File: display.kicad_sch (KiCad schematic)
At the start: 40 parts, among them J301 ConnectorLCDFrontLight, J302 FPC24(0.5MM), J303 FPC10(0.5MM), Q301 2N7002, Q302 2N7002, Q303 AO3401A

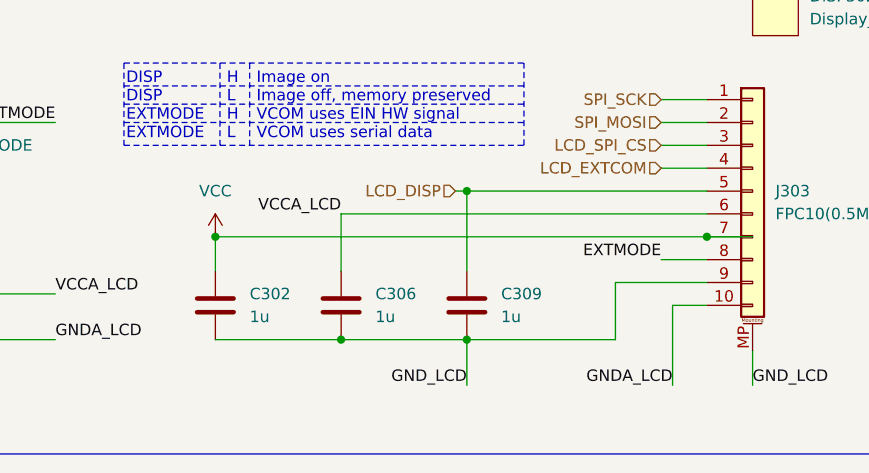
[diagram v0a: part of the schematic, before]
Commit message: schematic: fix LCD VCCA decoupling capacitor
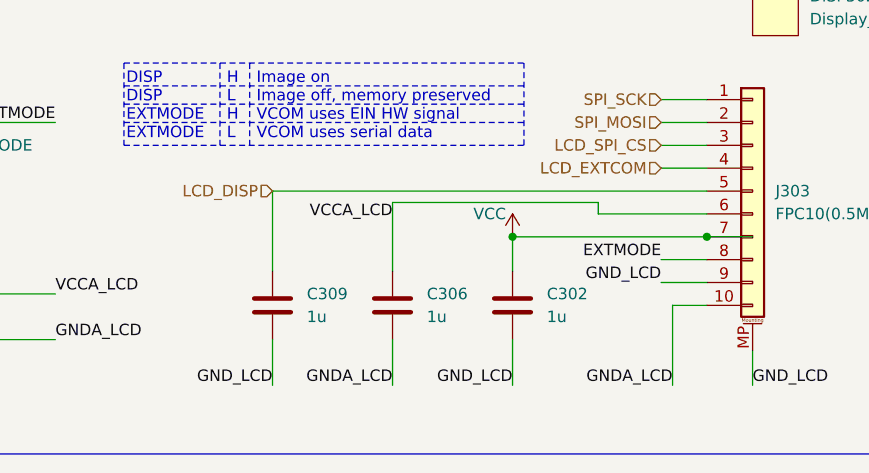
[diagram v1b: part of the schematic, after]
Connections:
- net GNDA_LCD: now also C306.2
- net LCD_CURRENT_SENSE: no longer C306.2
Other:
- moved on the sheet: C302, C306, C309

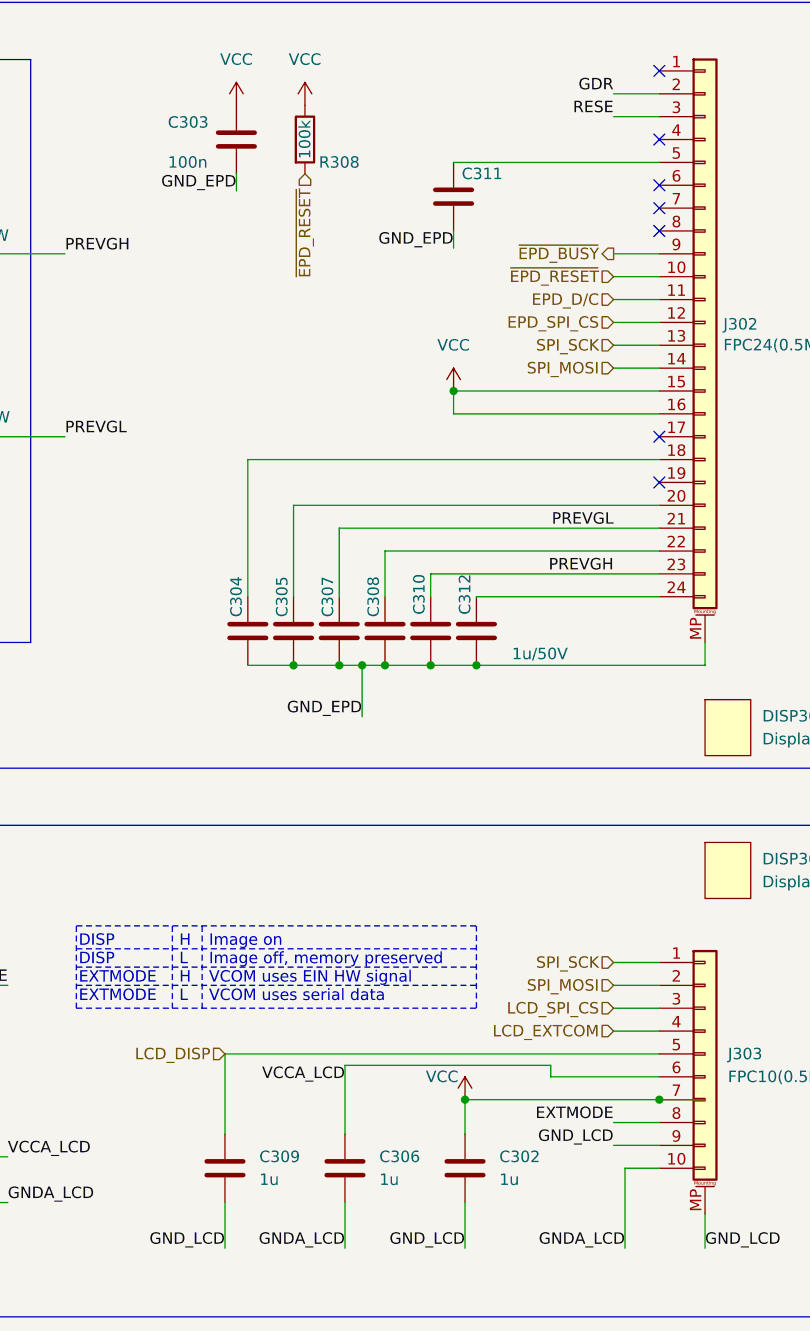
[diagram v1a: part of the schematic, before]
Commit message: Exchange brick-mount holes with actual footprint, connect holes to gnd
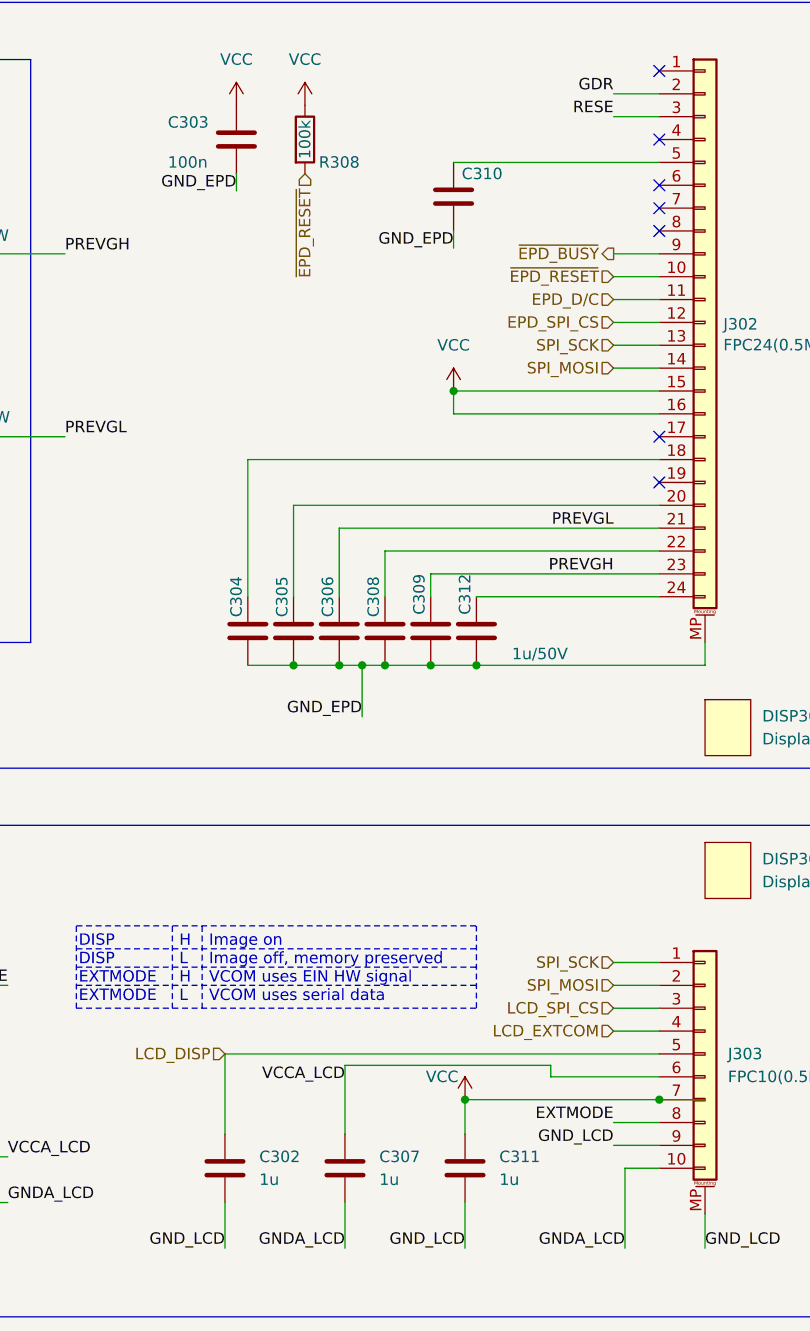
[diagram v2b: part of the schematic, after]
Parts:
- renumbered C309 to C302, C307 to C306, C306 to C307, C310 to C309, C311 to C310, C302 to C311
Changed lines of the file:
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@@
   (symbol (lib_id "Device:C") (at 215.265 148.59 0) (unit 1)
     (in_bom yes) (on_board yes)
-    (property "Reference" "C306" (id 0) (at 219.075 147.3199 0)
+    (property "Reference" "C307" (id 0) (at 219.075 147.3199 0)
       (effects (font (size 1.27 1.27)) (justify left))
     )
@@
   (symbol (lib_id "Device:C") (at 227.33 40.64 0) (unit 1)
     (in_bom yes) (on_board yes)
-    (property "Reference" "C311" (id 0) (at 230.505 38.1 0))
+    (property "Reference" "C310" (id 0) (at 230.505 38.1 0))
     (property "Value" "1u/50V" (id 1) (at 228.6 46.99 90)
       (effects (font (size 1.27 1.27)) hide)
@@
   (symbol (lib_id "Device:C") (at 224.79 88.9 180) (unit 1)
     (in_bom yes) (on_board yes)
-    (property "Reference" "C310" (id 0) (at 223.52 82.55 90)
+    (property "Reference" "C309" (id 0) (at 223.52 82.55 90)
       (effects (font (size 1.27 1.27)) (justify left))
     )
@@
   (symbol (lib_id "power:VCC") (at 228.6 140.97 0) (unit 1)
     (in_bom yes) (on_board yes)
-    (property "Reference" "#PWR0310" (id 0) (at 228.6 144.78 0)
+    (property "Reference" "#PWR0313" (id 0) (at 228.6 144.78 0)
       (effects (font (size 1.27 1.27)) hide)
     )
@@
   (symbol (lib_id "power:VCC") (at 227.33 62.23 0) (unit 1)
     (in_bom yes) (on_board yes) (fields_autoplaced)
-    (property "Reference" "#PWR0313" (id 0) (at 227.33 66.04 0)
+    (property "Reference" "#PWR0312" (id 0) (at 227.33 66.04 0)
       (effects (font (size 1.27 1.27)) hide)
     )
@@
   (symbol (lib_id "Device:C") (at 201.93 148.59 0) (unit 1)
     (in_bom yes) (on_board yes) (fields_autoplaced)
-    (property "Reference" "C309" (id 0) (at 205.74 147.3199 0)
+    (property "Reference" "C302" (id 0) (at 205.74 147.3199 0)
       (effects (font (size 1.27 1.27)) (justify left))
     )
@@
   (symbol (lib_id "Device:C") (at 214.63 88.9 180) (unit 1)
     (in_bom yes) (on_board yes)
-    (property "Reference" "C307" (id 0) (at 213.36 85.09 90))
+    (property "Reference" "C306" (id 0) (at 213.36 85.09 90))
     (property "Value" "1u/50V" (id 1) (at 213.36 82.55 90)
       (effects (font (size 1.27 1.27)) hide)
@@
   (symbol (lib_id "Device:C") (at 228.6 148.59 0) (unit 1)
     (in_bom yes) (on_board yes) (fields_autoplaced)
-    (property "Reference" "C302" (id 0) (at 232.41 147.3199 0)
+    (property "Reference" "C311" (id 0) (at 232.41 147.3199 0)
       (effects (font (size 1.27 1.27)) (justify left))
     )
@@
   (symbol (lib_id "power:VCC") (at 203.2 30.48 0) (unit 1)
     (in_bom yes) (on_board yes) (fields_autoplaced)
-    (property "Reference" "#PWR0311" (id 0) (at 203.2 34.29 0)
+    (property "Reference" "#PWR0310" (id 0) (at 203.2 34.29 0)
       (effects (font (size 1.27 1.27)) hide)
     )
@@
   (symbol (lib_id "power:VCC") (at 210.82 30.48 0) (unit 1)
     (in_bom yes) (on_board yes) (fields_autoplaced)
-    (property "Reference" "#PWR0312" (id 0) (at 210.82 34.29 0)
-      (effects (font (size 1.27 1.27)) hide)
-    )
+    (property "Reference" "#PWR0311" (id 0) (at 210.82 34.29 0)
+      (effects (font (size 1.27 1.27)) hide)
+    )

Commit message: Ficup column name for JLCPCB/LCSC part no
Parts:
- D301, D302, D303: LCSC (none) -> C965863
- D304, D305, D306: LCSC (none) -> C8598
- FB301, FB302: LCSC (none) -> C1017
- J301: LCSC (none) -> C11047
- J302: LCSC (none) -> C11057
- J303: LCSC (none) -> C11050
- L301: LCSC (none) -> C38117
- Q301, Q302: LCSC (none) -> C8545
- Q303: LCSC (none) -> C15127
- R301, R302: LCSC (none) -> C25271
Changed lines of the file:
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@@
+      (effects (font (size 1.27 1.27)) hide)
+    )
+    (property "LCSC" "C1017" (id 5) (at 168.91 152.4 0)
       (effects (font (size 1.27 1.27)) hide)
     )
@@
     )
     (property "JLCPCB" "C965863" (id 4) (at 78.105 62.23 0)
+      (effects (font (size 1.27 1.27)) hide)
+    )
+    (property "LCSC" "C965863" (id 5) (at 78.105 62.23 0)
       (effects (font (size 1.27 1.27)) hide)
     )
@@
       (effects (font (size 1.27 1.27)) hide)
     )
+    (property "LCSC" "C8598 " (id 5) (at 171.45 46.99 0)
+      (effects (font (size 1.27 1.27)) hide)
+    )
     (pin "1")
     (pin "2")
@@
     )
     (property "JLCPCB" "C11057" (id 4) (at 255.27 54.61 0)
+      (effects (font (size 1.27 1.27)) hide)
+    )
+    (property "LCSC" "C11057" (id 5) (at 255.27 54.61 0)
       (effects (font (size 1.27 1.27)) hide)
     )
@@
       (effects (font (size 1.27 1.27)) hide)
     )
+    (property "LCSC" "C8545" (id 5) (at 90.17 130.175 0)
+      (effects (font (size 1.27 1.27)) hide)
+    )
     (pin "1")
     (pin "2")
@@
       (effects (font (size 1.27 1.27)) hide)
     )
+    (property "LCSC" "C8598 " (id 5) (at 160.02 72.39 0)
+      (effects (font (size 1.27 1.27)) hide)
+    )
     (pin "1")
     (pin "2")
@@
     )
     (property "JLCPCB" "C11047" (id 4) (at 102.235 139.7 0)
+      (effects (font (size 1.27 1.27)) hide)
+    )
+    (property "LCSC" "C11047" (id 5) (at 102.235 139.7 0)
       (effects (font (size 1.27 1.27)) hide)
     )
@@
       (effects (font (size 1.27 1.27)) hide)
     )
+    (property "LCSC" "C15127" (id 5) (at 146.05 52.07 0)
+      (effects (font (size 1.27 1.27)) hide)
+    )
     (pin "1")
     (pin "2")
@@
     )
     (property "JLCPCB" "C965863" (id 4) (at 107.315 62.23 0)
+      (effects (font (size 1.27 1.27)) hide)
+    )
+    (property "LCSC" "C965863" (id 5) (at 107.315 62.23 0)
       (effects (font (size 1.27 1.27)) hide)
     )
@@
       (effects (font (size 1.27 1.27)) hide)
     )
+    (property "LCSC" "C25271" (id 5) (at 46.355 140.97 0)
+      (effects (font (size 1.27 1.27)) hide)
+    )
     (pin "1")
     (pin "2")
@@
     )
     (property "JLCPCB" "C965863" (id 4) (at 92.71 62.23 0)
+      (effects (font (size 1.27 1.27)) hide)
+    )
+    (property "LCSC" "C965863" (id 5) (at 92.71 62.23 0)
       (effects (font (size 1.27 1.27)) hide)
     )
@@
       (effects (font (size 1.27 1.27)) hide)
     )
+    (property "LCSC" "C25271" (id 5) (at 45.72 70.485 0)
+      (effects (font (size 1.27 1.27)) hide)
+    )
     (pin "1")
     (pin "2")
@@
     )
     (property "JLCPCB" "C11050" (id 4) (at 255.27 135.89 0)
+      (effects (font (size 1.27 1.27)) hide)
+    )
+    (property "LCSC" "C11050" (id 5) (at 255.27 135.89 0)
       (effects (font (size 1.27 1.27)) hide)
     )
@@
       (effects (font (size 1.27 1.27)) hide)
     )
+    (property "LCSC" "C8598 " (id 5) (at 171.45 67.31 0)
+      (effects (font (size 1.27 1.27)) hide)
+    )
     (pin "1")
     (pin "2")
@@
       (effects (font (size 1.27 1.27)) hide)
     )
+    (property "LCSC" "C8545" (id 5) (at 90.17 51.435 0)
+      (effects (font (size 1.27 1.27)) hide)
+    )
     (pin "1")
     (pin "2")
@@
     )
     (property "JLCPCB" "C1017" (id 4) (at 168.91 147.32 0)
+      (effects (font (size 1.27 1.27)) hide)
+    )
+    (property "LCSC" "C1017" (id 5) (at 168.91 147.32 0)
       (effects (font (size 1.27 1.27)) hide)
     )
@@
       (effects (font (size 1.27 1.27)) hide)
     )
+    (property "LCSC" "C38117" (id 5) (at 160.02 40.64 0)
+      (effects (font (size 1.27 1.27)) hide)
+    )

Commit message: Mark some parts as 'exclude from bom'
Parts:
- TP301, TP302: value TestPoint_2Pole -> TestPoint_3Pole; now left out of the parts list
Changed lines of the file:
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@@
   )
   (symbol (lib_id "project-lib:TestPoint_3Pole") (at 46.99 65.405 180) (unit 1)
-    (in_bom yes) (on_board yes)
+    (in_bom no) (on_board yes)
     (property "Reference" "TP301" (id 0) (at 46.99 60.325 0))
-    (property "Value" "TestPoint_2Pole" (id 1) (at 46.99 61.595 90)
+    (property "Value" "TestPoint_3Pole" (id 1) (at 46.99 61.595 90)
       (effects (font (size 1.27 1.27)) hide)
     )
@@
   )
   (symbol (lib_id "project-lib:TestPoint_3Pole") (at 47.625 135.89 180) (unit 1)
-    (in_bom yes) (on_board yes)
+    (in_bom no) (on_board yes)
     (property "Reference" "TP302" (id 0) (at 47.625 130.81 0))
-    (property "Value" "TestPoint_2Pole" (id 1) (at 47.625 132.08 90)
-      (effects (font (size 1.27 1.27)) hide)
-    )
+    (property "Value" "TestPoint_3Pole" (id 1) (at 47.625 132.08 90)
+      (effects (font (size 1.27 1.27)) hide)
+    )

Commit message: Components: select JLCPCB basic components
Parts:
- C301: footprint Capacitor_SMD:C_0805_2012Metric -> Capacitor_SMD:C_1206_3216Metric; LCSC (none) -> C29823
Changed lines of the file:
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@@
       (effects (font (size 1.27 1.27)) (justify left))
     )
-    (property "Footprint" "Capacitor_SMD:C_0805_2012Metric" (id 2) (at 160.9852 60.96 0)
+    (property "Footprint" "Capacitor_SMD:C_1206_3216Metric" (id 2) (at 160.9852 60.96 0)
       (effects (font (size 1.27 1.27)) hide)
     )
@@
       (effects (font (size 1.27 1.27)) hide)
     )
+    (property "LCSC" "C29823" (id 4) (at 160.02 57.15 0)
+      (effects (font (size 1.27 1.27)) hide)
+    )
